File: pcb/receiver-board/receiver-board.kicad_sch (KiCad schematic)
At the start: 0 parts

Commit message: Add receiver-board schematic and pcb
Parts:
- added J1: Conn_01x03_Socket, Connector_PinSocket_1.00mm:PinSocket_1x03_P1.00mm_Vertical, symbol Connector:Conn_01x03_Socket
- added U2: TSSP58038, OptoDevice:Vishay_MINICAST-3Pin, symbol Sensor_Proximity:TSSP58038
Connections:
- new net +3V3: J1.1 (Pin_1), U2.3 (Vs)
- new net GATE_TRIGGER2: J1.2 (Pin_2), U2.1 (OUT)
- new net GND: J1.3 (Pin_3), U2.2 (GND)

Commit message: receiver-board
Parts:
- J1: footprint Connector_PinSocket_1.00mm:PinSocket_1x03_P1.00mm_Vertical -> Connector_Audio:Jack_3.5mm_CUI_SJ-3523-SMT_Horizontal
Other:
- moved on the sheet: U2
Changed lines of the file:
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@@
 	(wire
 		(pts
-			(xy 133.35 71.12) (xy 130.81 71.12)
+			(xy 133.35 71.12) (xy 124.46 71.12)
 		)
 		(stroke
@@
 	(wire
 		(pts
-			(xy 130.81 66.04) (xy 135.89 66.04)
+			(xy 124.46 66.04) (xy 135.89 66.04)
 		)
 		(stroke
@@
 	(wire
 		(pts
-			(xy 130.81 60.96) (xy 133.35 60.96)
+			(xy 124.46 60.96) (xy 133.35 60.96)
 		)
 		(stroke
@@
 				)
 				(justify left)
+				(hide yes)
 			)
 		)
@@
 				)
 				(justify left)
-			)
-		)
-		(property "Footprint" "Connector_PinSocket_1.00mm:PinSocket_1x03_P1.00mm_Vertical"
+				(hide yes)
+			)
+		)
+		(property "Footprint" "Connector_Audio:Jack_3.5mm_CUI_SJ-3523-SMT_Horizontal"
 			(at 111.76 85.09 0)
 			(effects
@@
 	(symbol
 		(lib_id "Sensor_Proximity:TSSP58038")
-		(at 120.65 66.04 0)
+		(at 114.3 66.04 0)
 		(unit 1)
 		(exclude_from_sim no)
@@
 		(fields_autoplaced yes)
 		(property "Reference" "U2"
-			(at 118.915 54.61 0)
+			(at 112.565 54.61 0)
 			(effects
 				(font
@@
 		)
 		(property "Value" "TSSP58038"
-			(at 118.915 57.15 0)
+			(at 112.565 57.15 0)
 			(effects
 				(font
@@
 		)
 		(property "Footprint" "OptoDevice:Vishay_MINICAST-3Pin"
-			(at 119.38 75.565 0)
+			(at 113.03 75.565 0)
 			(effects
 				(font
@@
 		)
 		(property "Datasheet" "http://www.vishay.com/docs/82476/tssp58p38.pdf"
-			(at 137.16 58.42 0)
+			(at 130.81 58.42 0)
 			(effects
 				(font
@@
 		)
 		(property "Description" "IR Detector for Mid Range Proximity Sensor"
-			(at 120.65 66.04 0)
-			(effects
-				(font
+			(at 114.3 66.04 0)
+			(effects
+				(font

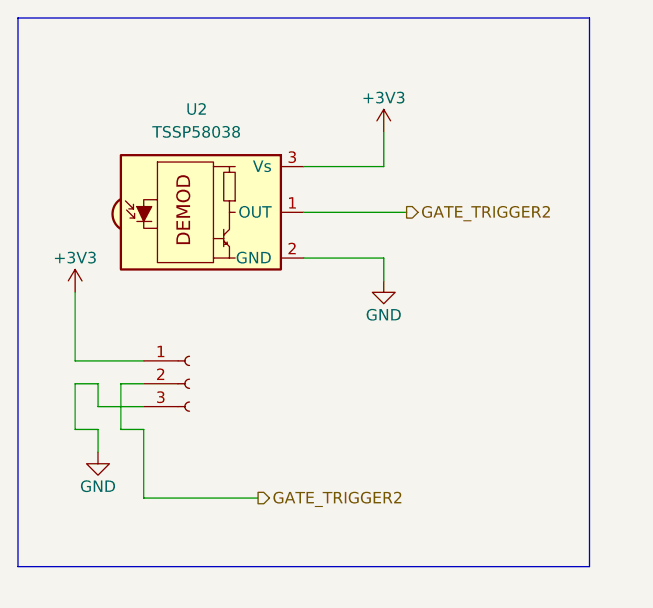
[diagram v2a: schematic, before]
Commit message: Added capacitor and changed jack on receiver board
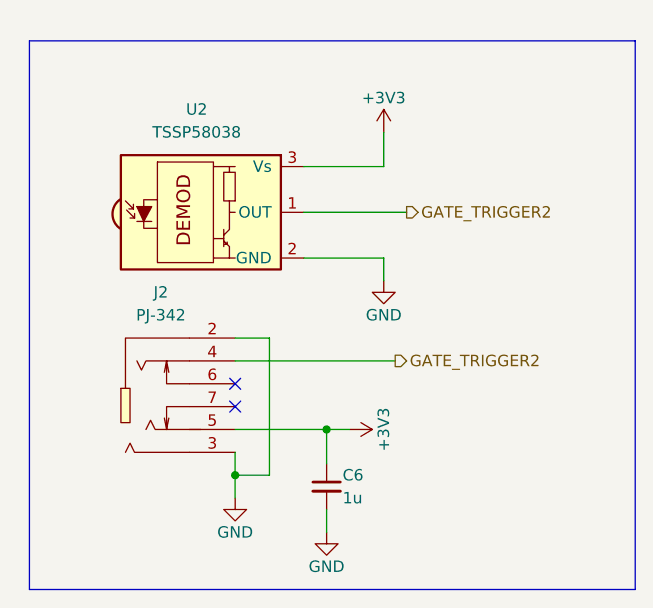
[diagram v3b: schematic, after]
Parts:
- removed J1: Conn_01x03_Socket, Connector_Audio:Jack_3.5mm_CUI_SJ-3523-SMT_Horizontal, symbol Connector:Conn_01x03_Socket
- added C6: C-1u-0402, Capacitor_SMD:C_0402_1005Metric, symbol DW-capacitors:C-1u-0402
- added J2: Jack_PJ-342, Connector_JAE:Jack_PJ-342, symbol DW-connectors:Jack_PJ-342
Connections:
- net +3V3: now also C6.1, J2.5
- net GATE_TRIGGER2: now also J2.4
- net GND: now also C6.2, J2.2, J2.3
- no-connect marks 0 -> 2
